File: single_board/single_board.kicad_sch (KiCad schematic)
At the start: 119 parts, among them J1 SWD, J11 SPI Debug, J17 BOOTSEL, J2 USB_C_Receptacle_USB2.0_16P, J3 RST, J30 JST_GH_H, J31 JST_GH_H, J32 PB_Vertical, J33 JST_GH_H, J34 PB_Vertical, J35 JST_GH_H, J36 JST_GH_H, J37 JST_GH_H, J38 PB_Vertical, J39 PB_Vertical, J4 Conn_01x02, J40 PB_Vertical, J41 PB_Vertical, J42 PB_Vertical, J43 PB_Vertical, J44 PB_Vertical, J45 PB_Vertical, J46 PB_Vertical, J47 PB_Vertical, J48 PB_Vertical, J49 PB_Vertical, J5 Conn_01x02, J51 JST_GH_H, Q1 AO3401A, Q2 AO3401A, Q3 AO3401A, Q4 AO3401A, Q5 2N7002, SW1 Button, U1 AP2112K-3.3, U3 USBLC6-2SC6, U4 LSM6DSV, U5 STM32G474VBTx, Y1 FC-135

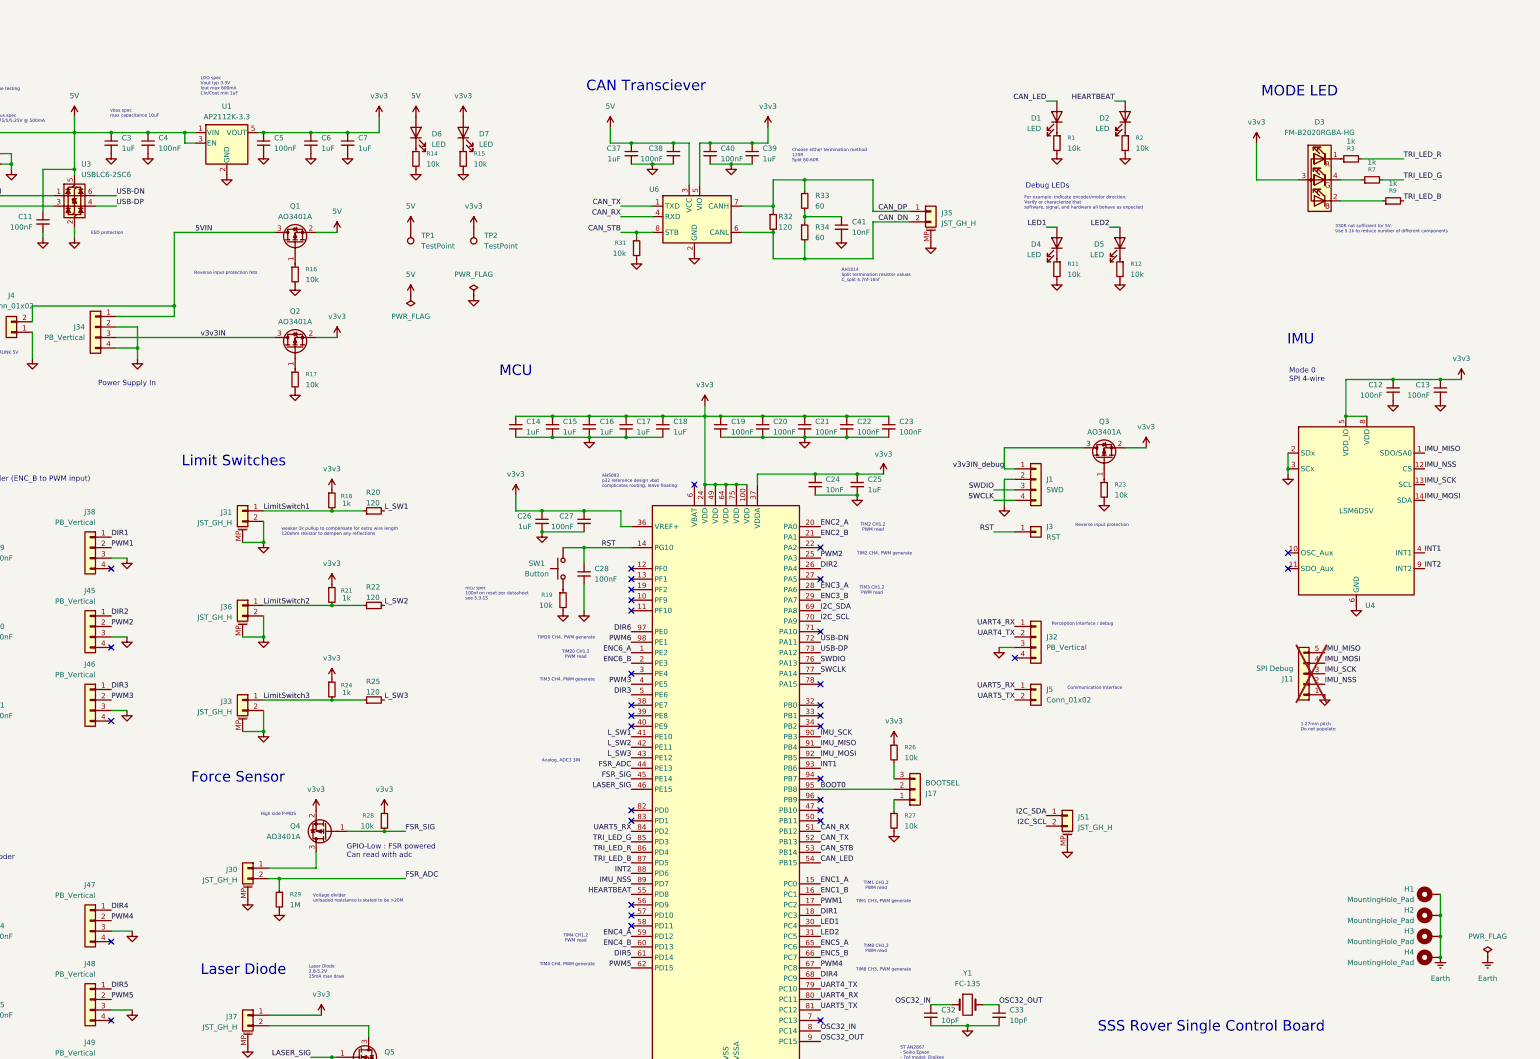
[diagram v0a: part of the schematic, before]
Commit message: Clear Routing
Clear previous routing, preparation for new picoblade and jst gh connectors
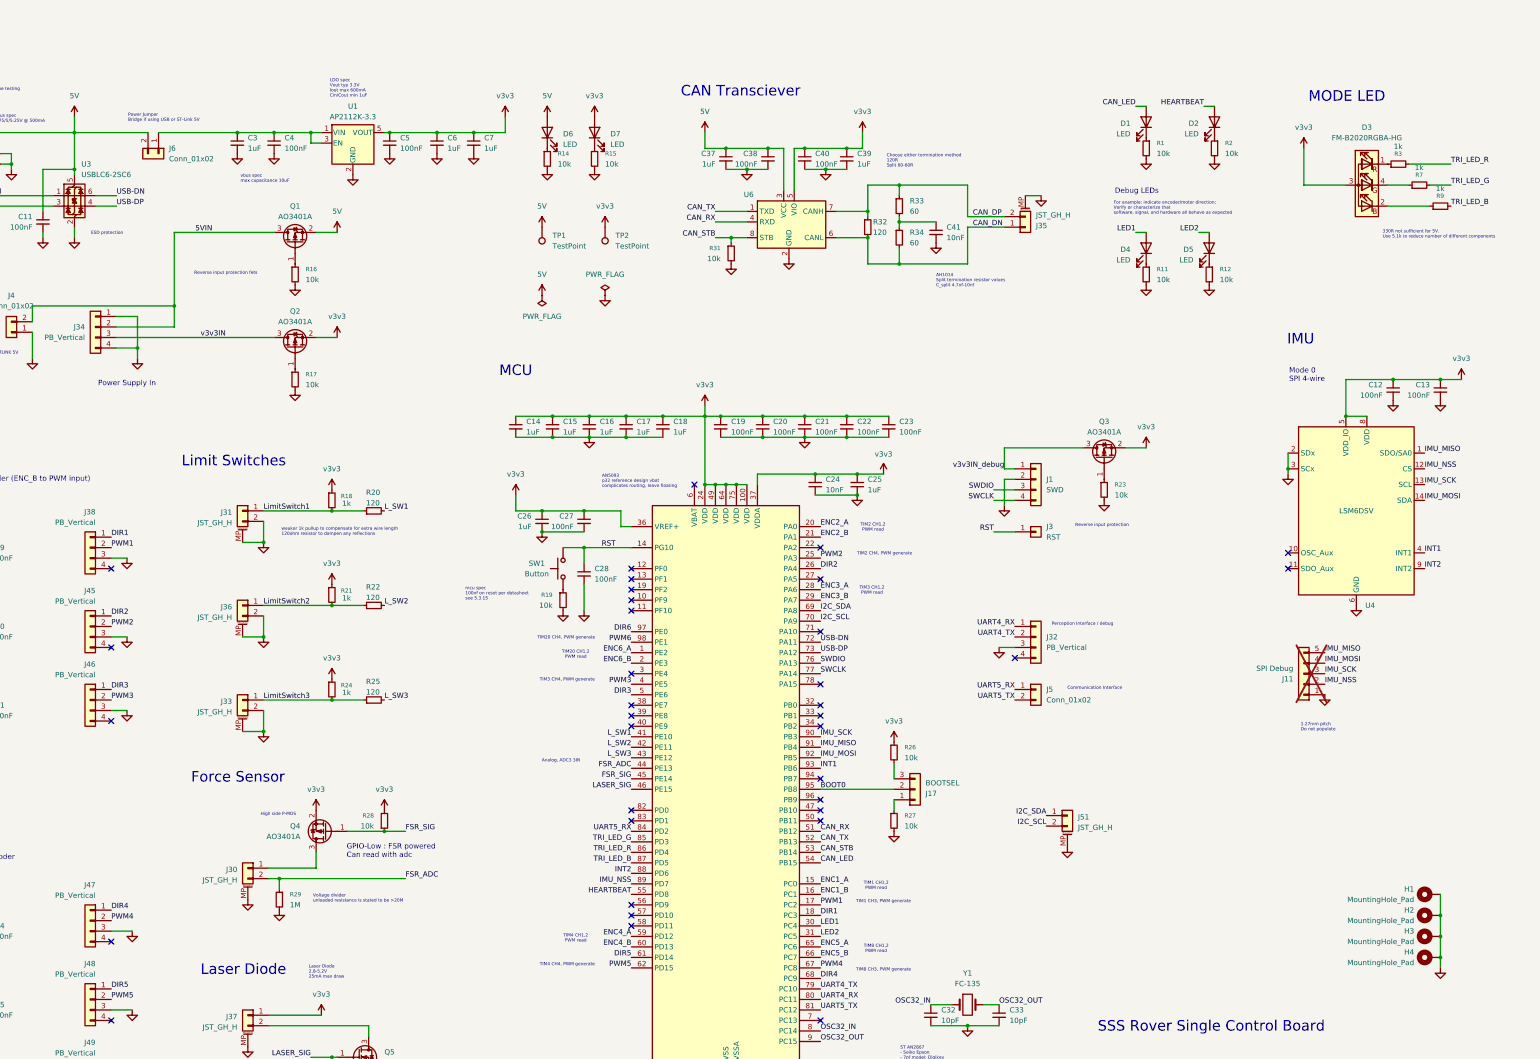
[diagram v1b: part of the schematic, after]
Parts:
- added J6: Conn_01x02, Connector_PinHeader_2.54mm:PinHeader_1x02_P2.54mm_Vertical, symbol Connector_Generic:Conn_01x02
- H1, H2, H3, H4: footprint MountingHole:MountingHole_5.3mm_M5_Pad -> MountingHole:MountingHole_3.2mm_M3_Pad_Via
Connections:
- net Earth is gone; now on net GND: H1.1, H2.1, H3.1, H4.1
- net 5V: now also J6.2 (Pin_2); no longer C3.1, C4.1, U1.1 (VIN), U1.3 (EN)
- net 5VIN: now also J34.2 (Pin_2); no longer J34.1 (Pin_1)
- net CAN_DN: now also J35.1 (Pin_1); no longer J35.2 (Pin_2)
- net CAN_DP: now also J35.2 (Pin_2); no longer J35.1 (Pin_1)
- net GND: now also J34.1 (Pin_1); no longer J34.2 (Pin_2)
- new net: C3.1, C4.1, J6.1 (Pin_1), U1.1 (VIN), U1.3 (EN)
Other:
- note added: "Power Jumper Bridge if using USB or ST-Link 5V"
- moved on the sheet: C3, C37, C38, C39, C4, C40, C41, C5, C6, C7, D1, D2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

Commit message: M8 mounting holes
better picoblade arrangement
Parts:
- H1, H2, H3, H4: footprint MountingHole:MountingHole_3.2mm_M3_Pad_Via -> MountingHole:MountingHole_8.4mm_M8_Pad_Via
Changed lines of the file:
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@@
 			)
 		)
-		(property "Footprint" "MountingHole:MountingHole_3.2mm_M3_Pad_Via"
+		(property "Footprint" "MountingHole:MountingHole_8.4mm_M8_Pad_Via"
 			(at 397.51 222.25 0)
 			(hide yes)
@@
 			)
 		)
-		(property "Footprint" "MountingHole:MountingHole_3.2mm_M3_Pad_Via"
+		(property "Footprint" "MountingHole:MountingHole_8.4mm_M8_Pad_Via"
 			(at 397.51 227.33 0)
 			(hide yes)
@@
 			)
 		)
-		(property "Footprint" "MountingHole:MountingHole_3.2mm_M3_Pad_Via"
+		(property "Footprint" "MountingHole:MountingHole_8.4mm_M8_Pad_Via"
 			(at 397.51 212.09 0)
 			(hide yes)
@@
 			)
 		)
-		(property "Footprint" "MountingHole:MountingHole_3.2mm_M3_Pad_Via"
+		(property "Footprint" "MountingHole:MountingHole_8.4mm_M8_Pad_Via"
 			(at 397.51 217.17 0)
 			(hide yes)

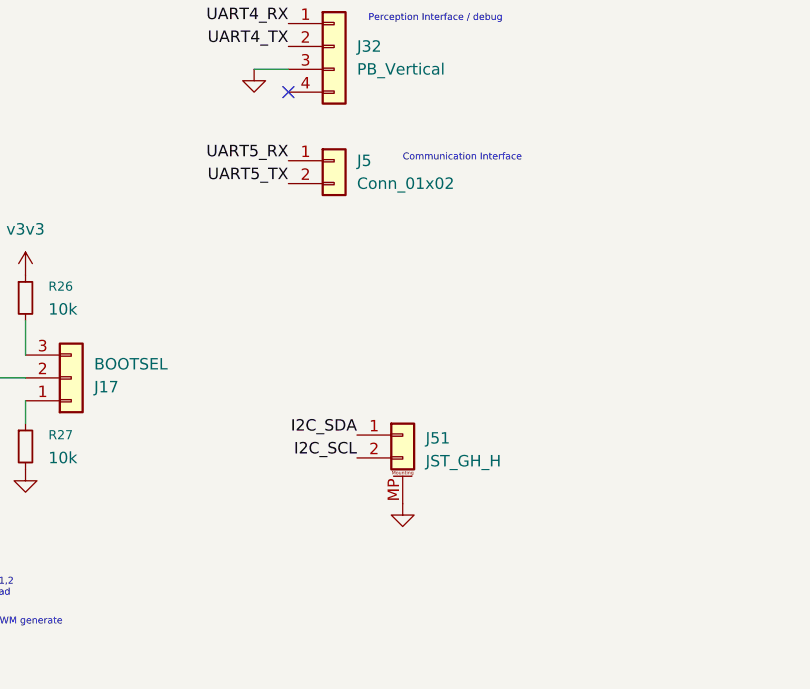
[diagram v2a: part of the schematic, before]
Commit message: Updated connectors
2MMCX for comms uart, picoblade for i2c
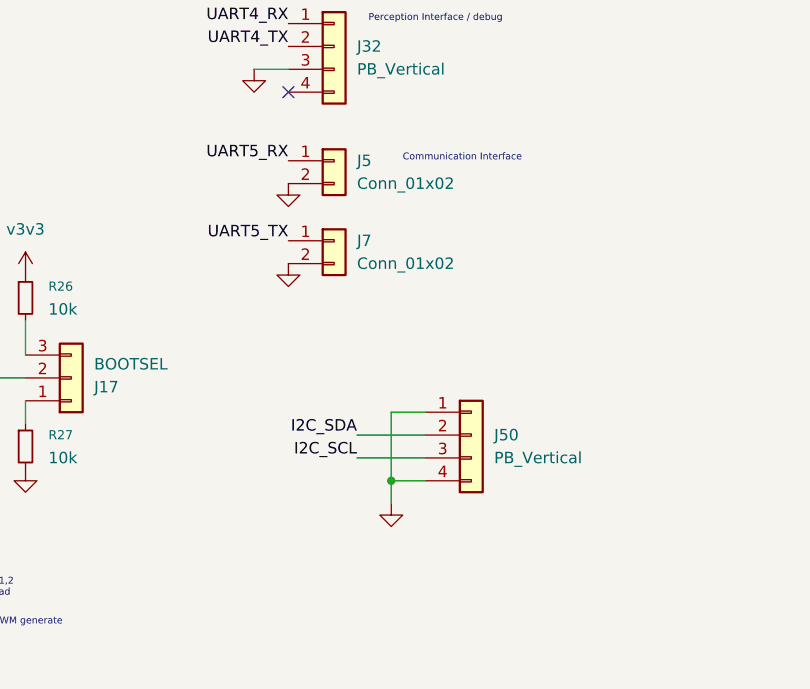
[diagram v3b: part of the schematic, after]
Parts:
- removed J51: JST_GH_H, Connector_JST:JST_GH_SM02B-GHS-TB_1x02-1MP_P1.25mm_Horizontal, symbol Connector_Generic_MountingPin:Conn_01x02_MountingPin
- added J50: PB_Vertical, Connector_Molex:Molex_PicoBlade_53047-0410_1x04_P1.25mm_Vertical, symbol Connector_Generic:Conn_01x04
- added J7: Conn_01x02, Connector_Coaxial:MMCX_Molex_73415-0961_Horizontal_0.8mm-PCB, symbol Connector_Generic:Conn_01x02
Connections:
- net GND: now also J5.2 (Pin_2), J50.1 (Pin_1), J50.4 (Pin_4), J7.2 (Pin_2)
- net I2C_SCL: now also J50.3 (Pin_3)
- net I2C_SDA: now also J50.2 (Pin_2)
- net UART5_TX: now also J7.1 (Pin_1); no longer J5.2 (Pin_2)

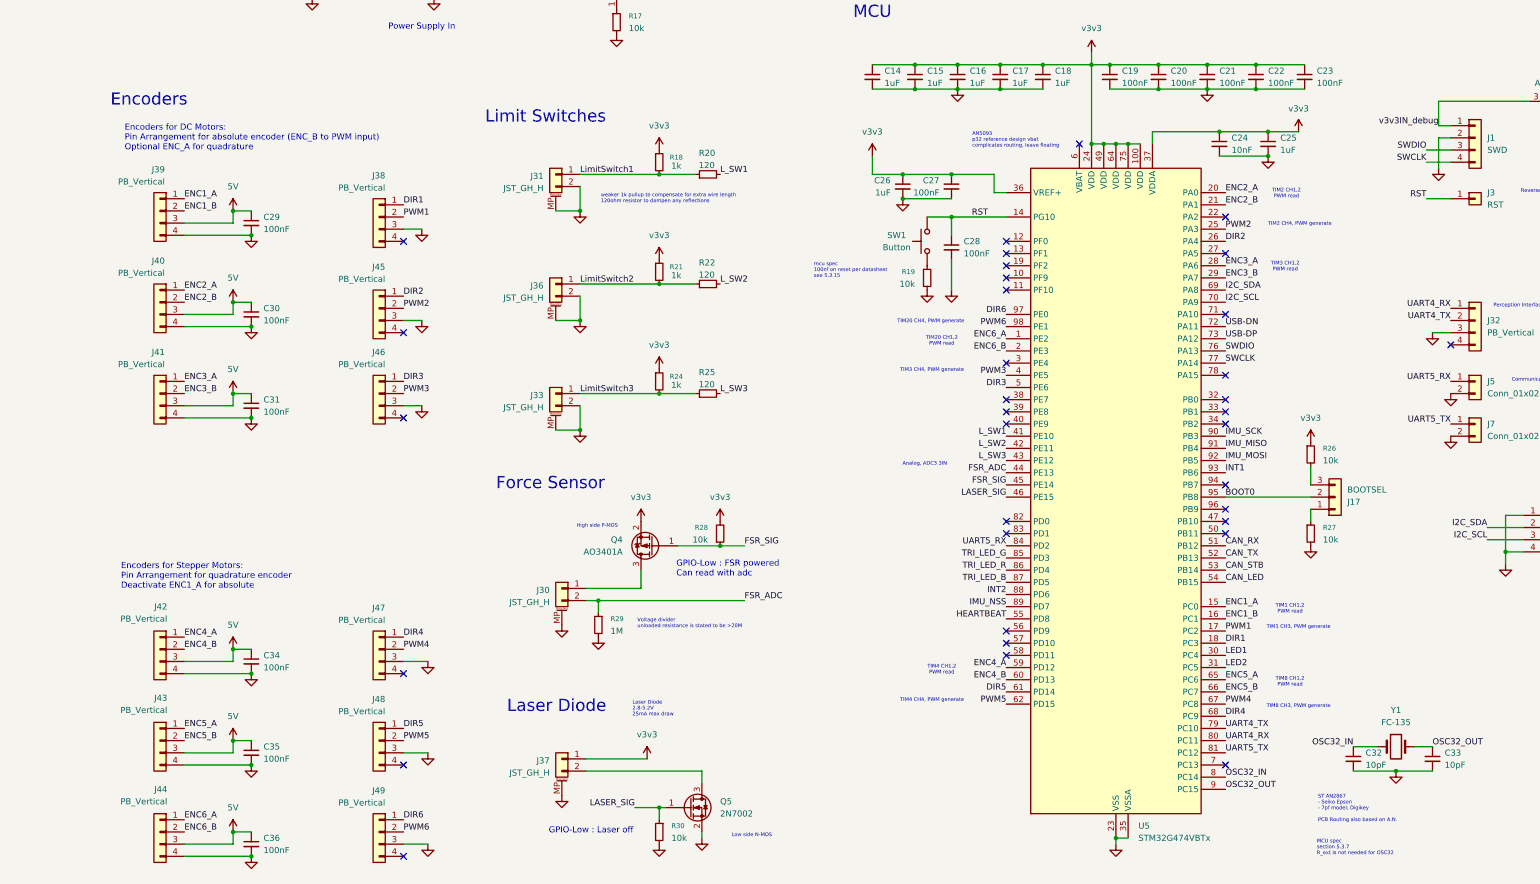
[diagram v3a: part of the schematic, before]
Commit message: Adjust connector pinouts
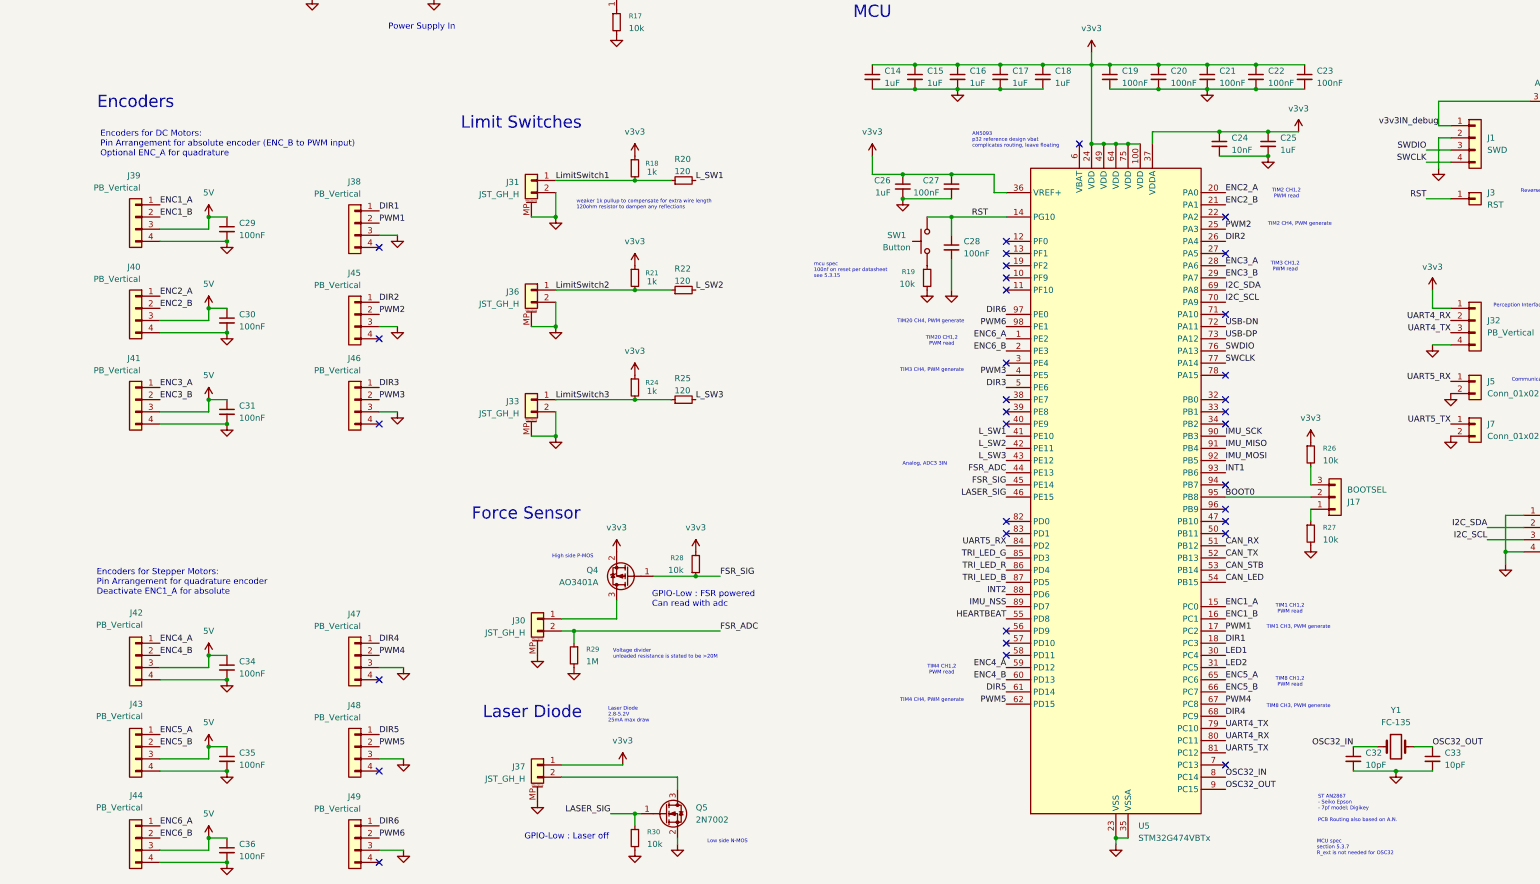
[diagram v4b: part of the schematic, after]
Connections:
- net GND: now also J32.4 (Pin_4); no longer J32.3 (Pin_3)
- net UART4_RX: now also J32.2 (Pin_2); no longer J32.1 (Pin_1)
- net UART4_TX: now also J32.3 (Pin_3); no longer J32.2 (Pin_2)
- net v3v3: now also J32.1 (Pin_1)
- no-connect marks 38 -> 37
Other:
- moved on the sheet: C29, C30, C31, C34, C35, C36, J30, J31, J33, J36, J37, J38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

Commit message: PCB Layout
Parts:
- removed R32: 120, Resistor_SMD:R_0402_1005Metric, symbol Device:R_Small
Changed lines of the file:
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@@
 	)
 	(junction
-		(at 261.62 53.34)
-		(diameter 0)
-		(color 0 0 0 0)
-	)
-	(junction
 		(at 38.1 257.81)
 		(diameter 0)
@@
 	)
 	(junction
-		(at 261.62 46.99)
-		(diameter 0)
-		(color 0 0 0 0)
-	)
-	(junction
 		(at 41.91 243.84)
 		(diameter 0)
@@
 	(wire
 		(pts
-			(xy 261.62 46.99) (xy 261.62 48.26)
-		)
-		(stroke
-			(width 0)
-			(type default)
-		)
-	)
-	(wire
-		(pts
 			(xy 294.64 109.22) (xy 297.18 109.22)
 		)
@@
 					(unit 1)
 				)
-			)
-		)
-	)
-	(symbol
-		(lib_id "Device:R_Small")
-		(at 261.62 50.8 0)
-		(unit 1)
-		(body_style 1)
-		(exclude_from_sim no)
-		(in_bom yes)
-		(on_board yes)
-		(in_pos_files yes)
-		(dnp no)
-		(property "Reference" "R32"
-			(at 262.89 49.5299 0)
-			(show_name no)
-			(do_not_autoplace no)
-			(effects
-				(font
-					(size 1.27 1.27)
-				)
-				(justify left)
-			)
-		)
-		(property "Value" "120"
-			(at 262.89 52.0699 0)
-			(show_name no)
-			(do_not_autoplace no)
-			(effects
-				(font
-					(size 1.27 1.27)
-				)
-				(justify left)
-			)
-		)
-		(property "Footprint" "Resistor_SMD:R_0402_1005Metric"
-			(at 261.62 50.8 0)
-			(hide yes)
-			(show_name no)
-			(do_not_autoplace no)
-			(effects
-				(font
-					(size 1.27 1.27)
-				)
-			)
-		)
-		(property "Datasheet" ""
-			(at 261.62 50.8 0)
-			(hide yes)
-			(show_name no)
-			(do_not_autoplace no)
-			(effects
-				(font
-					(size 1.27 1.27)
-				)
-			)
-		)
-		(property "Description" "Resistor, small symbol"
-			(at 261.62 50.8 0)
-			(hide yes)
-			(show_name no)
-			(do_not_autoplace no)
-			(effects
-				(font
-					(size 1.27 1.27)
-				)
-			)
-		)
-		(pin "1"
-		)
-		(pin "2"
-		)
-		(instances
-			(project "single_board"
-				(path "/ae10586e-ebf8-402d-a979-c2f011cdeee2"
-					(reference "R32")
-					(unit 1)
-				)
